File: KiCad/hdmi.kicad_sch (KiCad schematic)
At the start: 32 parts, among them J25 HDMI_A, Q1 2N7002, Q2 2N7002, Q3 2N7002, U20 H5VU25U, U21 H5VU25U, U22 H5VU25U

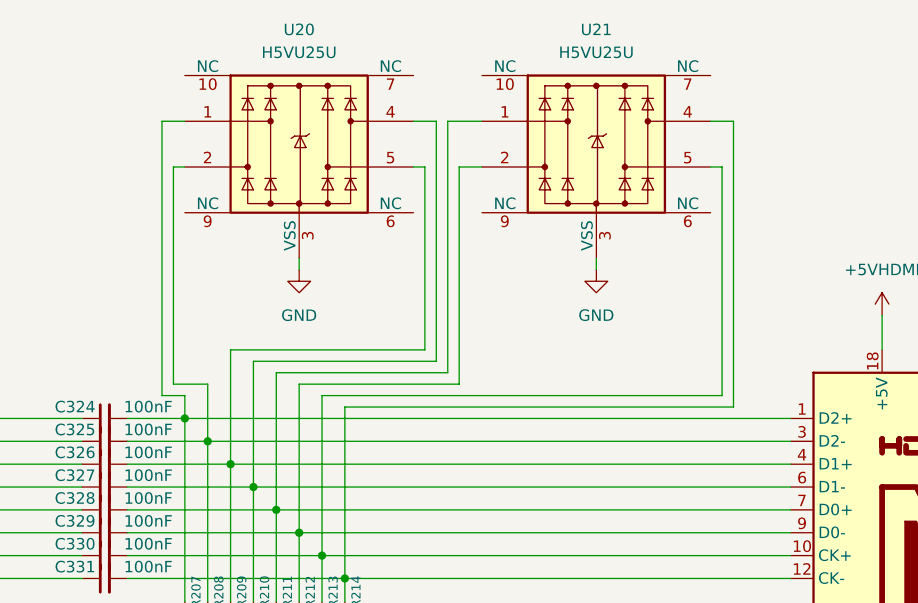
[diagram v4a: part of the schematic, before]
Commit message: Fix esd diodes, add some footprints.
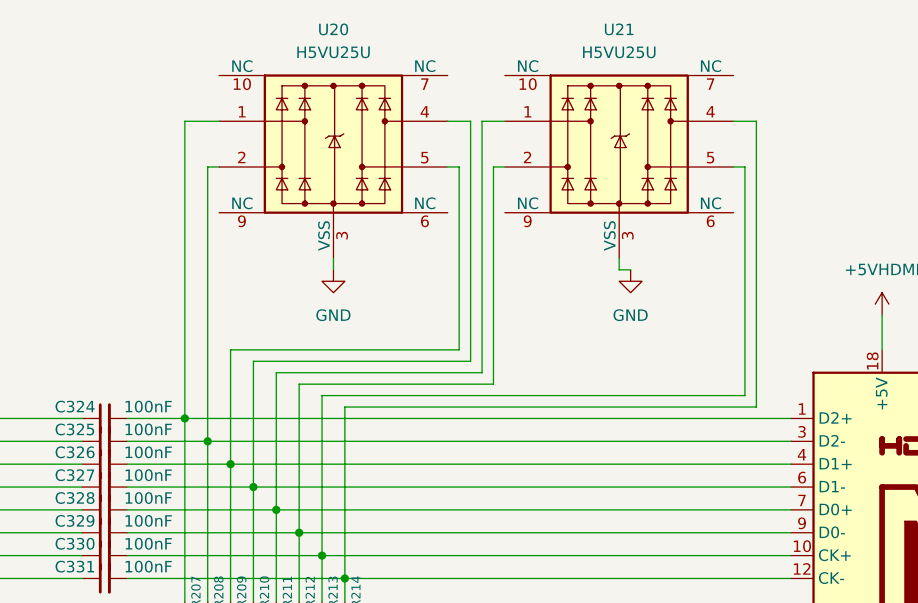
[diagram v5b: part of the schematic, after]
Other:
- moved on the sheet: U20, U21
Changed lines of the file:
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@@
 	(wire
 		(pts
-			(xy 198.12 62.23) (xy 198.12 63.5)
+			(xy 200.66 62.23) (xy 200.66 63.5)
 		)
 		(stroke
@@
 	(wire
 		(pts
-			(xy 181.61 74.93) (xy 162.56 74.93)
+			(xy 185.42 74.93) (xy 162.56 74.93)
 		)
 		(stroke
@@
 	(wire
 		(pts
-			(xy 212.09 77.47) (xy 167.64 77.47)
+			(xy 214.63 77.47) (xy 167.64 77.47)
+		)
+		(stroke
+			(width 0)
+			(type default)
+		)
+	)
+	(wire
+		(pts
+			(xy 200.66 63.5) (xy 201.93 63.5)
 		)
 		(stroke
@@
 	(wire
 		(pts
-			(xy 179.07 52.07) (xy 179.07 72.39)
+			(xy 182.88 52.07) (xy 182.88 72.39)
 		)
 		(stroke
@@
 	(wire
 		(pts
-			(xy 185.42 46.99) (xy 181.61 46.99)
+			(xy 187.96 46.99) (xy 185.42 46.99)
 		)
 		(stroke
@@
 	(wire
 		(pts
-			(xy 149.86 77.47) (xy 152.4 77.47)
-		)
-		(stroke
-			(width 0)
-			(type default)
-		)
-	)
-	(wire
-		(pts
 			(xy 146.05 97.79) (xy 170.18 97.79)
 		)
@@
 	(wire
 		(pts
-			(xy 177.8 52.07) (xy 179.07 52.07)
+			(xy 181.61 52.07) (xy 182.88 52.07)
 		)
 		(stroke
@@
 	(wire
 		(pts
-			(xy 179.07 72.39) (xy 157.48 72.39)
+			(xy 182.88 72.39) (xy 157.48 72.39)
 		)
 		(stroke
@@
 	(wire
 		(pts
-			(xy 210.82 46.99) (xy 213.36 46.99)
+			(xy 213.36 46.99) (xy 215.9 46.99)
 		)
 		(stroke
@@
 	(wire
 		(pts
-			(xy 152.4 77.47) (xy 152.4 80.01)
+			(xy 152.4 46.99) (xy 152.4 80.01)
 		)
 		(stroke
@@
 	(wire
 		(pts
-			(xy 213.36 46.99) (xy 213.36 78.74)
+			(xy 215.9 46.99) (xy 215.9 78.74)
 		)
 		(stroke
@@
 	(wire
 		(pts
-			(xy 149.86 46.99) (xy 149.86 77.47)
-		)
-		(stroke
-			(width 0)
-			(type default)
-		)
-	)
-	(wire
-		(pts
-			(xy 180.34 46.99) (xy 180.34 73.66)
+			(xy 184.15 46.99) (xy 184.15 73.66)
 		)
 		(stroke
@@
 	(wire
 		(pts
-			(xy 181.61 46.99) (xy 181.61 74.93)
+			(xy 185.42 46.99) (xy 185.42 74.93)
 		)
 		(stroke
@@
 	(wire
 		(pts
-			(xy 180.34 73.66) (xy 160.02 73.66)
+			(xy 184.15 73.66) (xy 160.02 73.66)
 		)
 		(stroke
@@
 	(wire
 		(pts
-			(xy 182.88 52.07) (xy 182.88 76.2)
+			(xy 186.69 52.07) (xy 186.69 76.2)
 		)
 		(stroke
@@
 	(wire
 		(pts
-			(xy 151.13 52.07) (xy 151.13 76.2)
-		)
-		(stroke
-			(width 0)
-			(type default)
-		)
-	)
-	(wire
-		(pts
-			(xy 185.42 52.07) (xy 182.88 52.07)
+			(xy 187.96 52.07) (xy 186.69 52.07)
 		)
 		(stroke
@@
 	(wire
 		(pts
-			(xy 165.1 62.23) (xy 165.1 63.5)
+			(xy 168.91 62.23) (xy 168.91 63.5)
 		)
 		(stroke
@@
 	(wire
 		(pts
-			(xy 151.13 76.2) (xy 154.94 76.2)
-		)
-		(stroke
-			(width 0)
-			(type default)
-		)
-	)
-	(wire
-		(pts
-			(xy 154.94 76.2) (xy 154.94 82.55)
+			(xy 154.94 52.07) (xy 154.94 82.55)
 		)
 		(stroke
@@
 	(wire
 		(pts
-			(xy 152.4 52.07) (xy 151.13 52.07)
+			(xy 156.21 52.07) (xy 154.94 52.07)
 		)
 		(stroke
@@
 	(wire
 		(pts
-			(xy 152.4 46.99) (xy 149.86 46.99)
+			(xy 156.21 46.99) (xy 152.4 46.99)
 		)
 		(stroke
@@
 	(wire
 		(pts
-			(xy 177.8 46.99) (xy 180.34 46.99)
+			(xy 181.61 46.99) (xy 184.15 46.99)
 		)
 		(stroke
@@
 	(wire
 		(pts
-			(xy 212.09 52.07) (xy 212.09 77.47)
+			(xy 214.63 52.07) (xy 214.63 77.47)
 		)
 		(stroke
@@
 	(wire
 		(pts
-			(xy 210.82 52.07) (xy 212.09 52.07)
+			(xy 213.36 52.07) (xy 214.63 52.07)
 		)
 		(stroke
@@
 	(wire
 		(pts
-			(xy 182.88 76.2) (xy 165.1 76.2)
+			(xy 186.69 76.2) (xy 165.1 76.2)
 		)
 		(stroke
@@
 	(wire
 		(pts
-			(xy 213.36 78.74) (xy 170.18 78.74)
+			(xy 215.9 78.74) (xy 170.18 78.74)
 		)
 		(stroke
@@
 	(symbol
 		(lib_id "power:GND")
-		(at 198.12 63.5 0)
+		(at 201.93 63.5 0)
 		(unit 1)
 		(exclude_from_sim no)
@@
 		(fields_autoplaced yes)
 		(property "Reference" "#PWR0317"
-			(at 198.12 69.85 0)
+			(at 201.93 69.85 0)
 			(effects
 				(font
@@
 		)
 		(property "Value" "GND"
-			(at 198.12 68.58 0)
+			(at 201.93 68.58 0)
 			(effects
 				(font
@@
 		)
 		(property "Footprint" ""
-			(at 198.12 63.5 0)
+			(at 201.93 63.5 0)
 			(effects
 				(font
@@
 		)
 		(property "Datasheet" ""
-			(at 198.12 63.5 0)
+			(at 201.93 63.5 0)
 			(effects
 				(font
@@
 		)
 		(property "Description" "Power symbol creates a global label with name \"GND\" , ground"
-			(at 198.12 63.5 0)
+			(at 201.93 63.5 0)
 			(effects
 				(font
@@
 	(symbol
 		(lib_id "Power_Protection:D3V3XA4B10LP")
-		(at 165.1 49.53 0)
+		(at 168.91 49.53 0)
 		(unit 1)
 		(exclude_from_sim no)
@@
 		(fields_autoplaced yes)
 		(property "Reference" "U20"
-			(at 165.1 36.83 0)
+			(at 168.91 36.83 0)
 			(effects
 				(font
@@
 		)
 		(property "Value" "H5VU25U"
-			(at 165.1 39.37 0)
+			(at 168.91 39.37 0)
 			(effects
 				(font
@@
 		)
 		(property "Footprint" "Package_DFN_QFN:Diodes_UDFN-10_1.0x2.5mm_P0.5mm"
-			(at 140.97 59.69 0)
+			(at 144.78 59.69 0)
 			(effects
 				(font
@@
 		)
 		(property "Datasheet" "https://www.diodes.com/assets/Datasheets/D3V3XA4B10LP.pdf"
-			(at 165.1 49.53 0)
+			(at 168.91 49.53 0)
 			(effects
 				(font
@@
 		)
 		(property "Description" "4-Channel Low Capacitance TVS Diode Array, DFN-10"
-			(at 165.1 49.53 0)
+			(at 168.91 49.53 0)
 			(effects
 				(font
@@
 	(symbol
 		(lib_id "Power_Protection:D3V3XA4B10LP")
-		(at 198.12 49.53 0)
+		(at 200.66 49.53 0)
 		(unit 1)
 		(exclude_from_sim no)
@@
 		(fields_autoplaced yes)
 		(property "Reference" "U21"
-			(at 198.12 36.83 0)
+			(at 200.66 36.83 0)
 			(effects
 				(font
@@
 		)
 		(property "Value" "H5VU25U"
-			(at 198.12 39.37 0)
+			(at 200.66 39.37 0)
 			(effects
 				(font
@@
 		)
 		(property "Footprint" "Package_DFN_QFN:Diodes_UDFN-10_1.0x2.5mm_P0.5mm"
-			(at 173.99 59.69 0)
+			(at 176.53 59.69 0)
 			(effects
 				(font
@@
 		)
 		(property "Datasheet" "https://www.diodes.com/assets/Datasheets/D3V3XA4B10LP.pdf"
-			(at 198.12 49.53 0)
+			(at 200.66 49.53 0)
 			(effects
 				(font
@@
 		)
 		(property "Description" "4-Channel Low Capacitance TVS Diode Array, DFN-10"
-			(at 198.12 49.53 0)
+			(at 200.66 49.53 0)
 			(effects
 				(font
@@
 	(symbol
 		(lib_id "power:GND")
-		(at 165.1 63.5 0)
+		(at 168.91 63.5 0)
 		(unit 1)
 		(exclude_from_sim no)
@@
 		(fields_autoplaced yes)
 		(property "Reference" "#PWR0316"
-			(at 165.1 69.85 0)
+			(at 168.91 69.85 0)
 			(effects
 				(font
@@
 		)
 		(property "Value" "GND"
-			(at 165.1 68.58 0)
+			(at 168.91 68.58 0)
 			(effects
 				(font
@@
 		)
 		(property "Footprint" ""
-			(at 165.1 63.5 0)
+			(at 168.91 63.5 0)
 			(effects
 				(font
@@
 		)
 		(property "Datasheet" ""
-			(at 165.1 63.5 0)
+			(at 168.91 63.5 0)
 			(effects
 				(font
@@
 		)
 		(property "Description" "Power symbol creates a global label with name \"GND\" , ground"
-			(at 165.1 63.5 0)
+			(at 168.91 63.5 0)
 			(effects
 				(font

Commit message: Lots of tiny capacitors
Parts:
- C323, C324, C325, C326, C327, C328, C329, C330, C331: footprint (none) -> Capacitor_SMD:C_0402_1005Metric
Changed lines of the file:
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@@
 			)
 		)
-		(property "Footprint" ""
+		(property "Footprint" "Capacitor_SMD:C_0402_1005Metric"
 			(at 143.51 85.09 0)
 			(effects
@@
 			)
 		)
-		(property "Footprint" ""
+		(property "Footprint" "Capacitor_SMD:C_0402_1005Metric"
 			(at 143.51 80.01 0)
 			(effects
@@
 			)
 		)
-		(property "Footprint" ""
+		(property "Footprint" "Capacitor_SMD:C_0402_1005Metric"
 			(at 143.51 90.17 0)
 			(effects
@@
 			)
 		)
-		(property "Footprint" ""
+		(property "Footprint" "Capacitor_SMD:C_0402_1005Metric"
 			(at 143.51 82.55 0)
 			(effects
@@
 			)
 		)
-		(property "Footprint" ""
+		(property "Footprint" "Capacitor_SMD:C_0402_1005Metric"
 			(at 143.51 87.63 0)
 			(effects
@@
 			)
 		)
-		(property "Footprint" ""
+		(property "Footprint" "Capacitor_SMD:C_0402_1005Metric"
 			(at 62.23 97.79 0)
 			(effects
@@
 			)
 		)
-		(property "Footprint" ""
+		(property "Footprint" "Capacitor_SMD:C_0402_1005Metric"
 			(at 143.51 92.71 0)
 			(effects
@@
 			)
 		)
-		(property "Footprint" ""
+		(property "Footprint" "Capacitor_SMD:C_0402_1005Metric"
 			(at 143.51 95.25 0)
 			(effects
@@
 			)
 		)
-		(property "Footprint" ""
+		(property "Footprint" "Capacitor_SMD:C_0402_1005Metric"
 			(at 143.51 97.79 0)
 			(effects

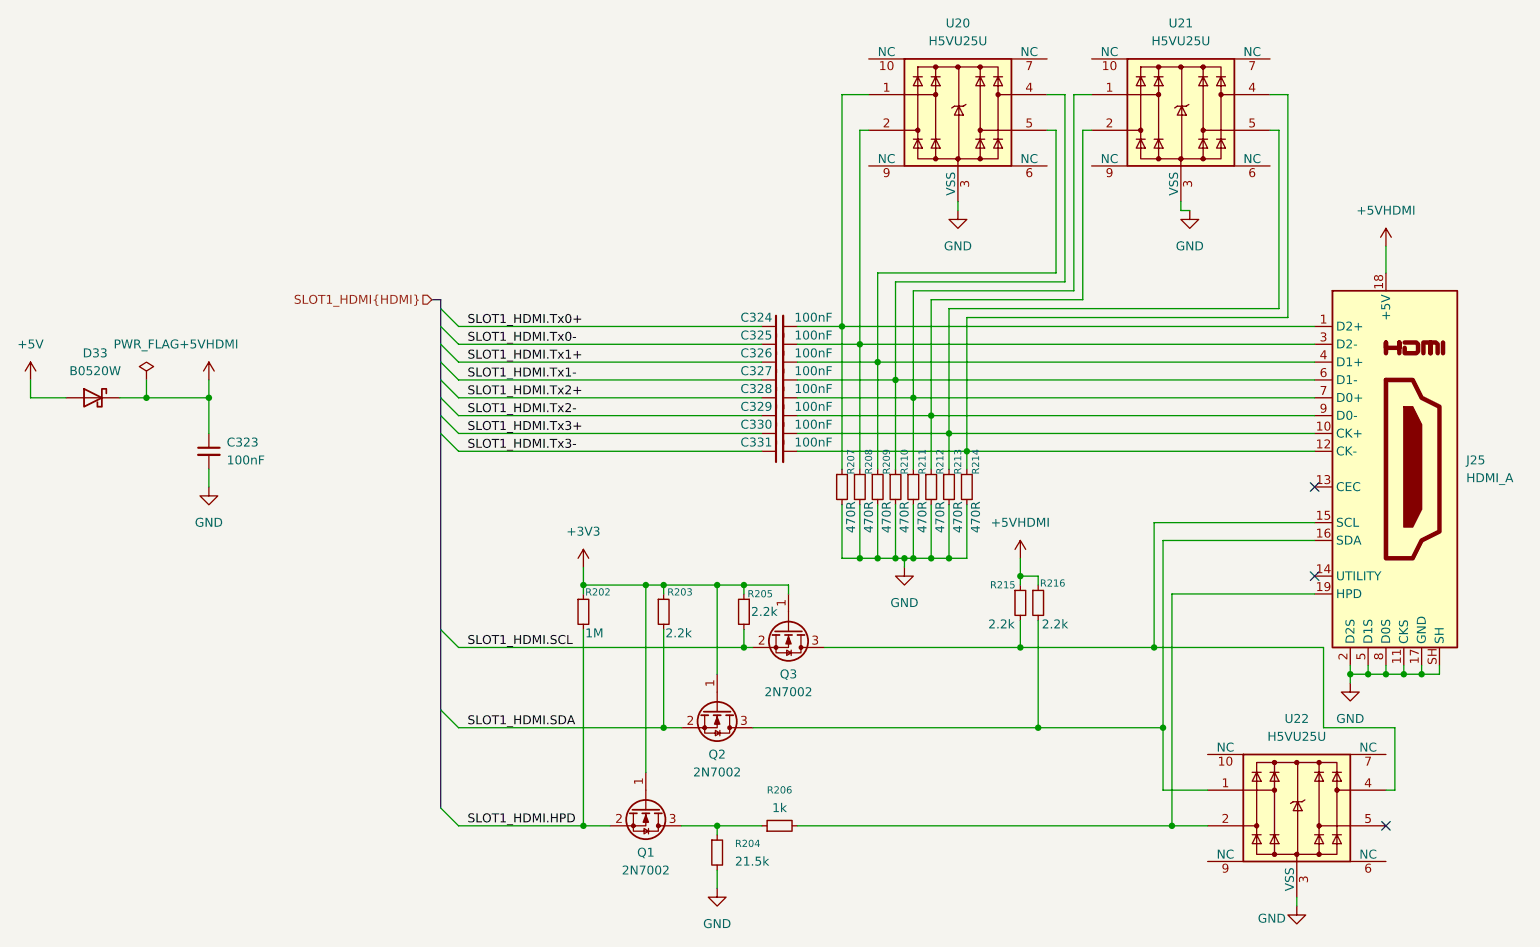
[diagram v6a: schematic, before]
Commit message: Add most passive component footprints
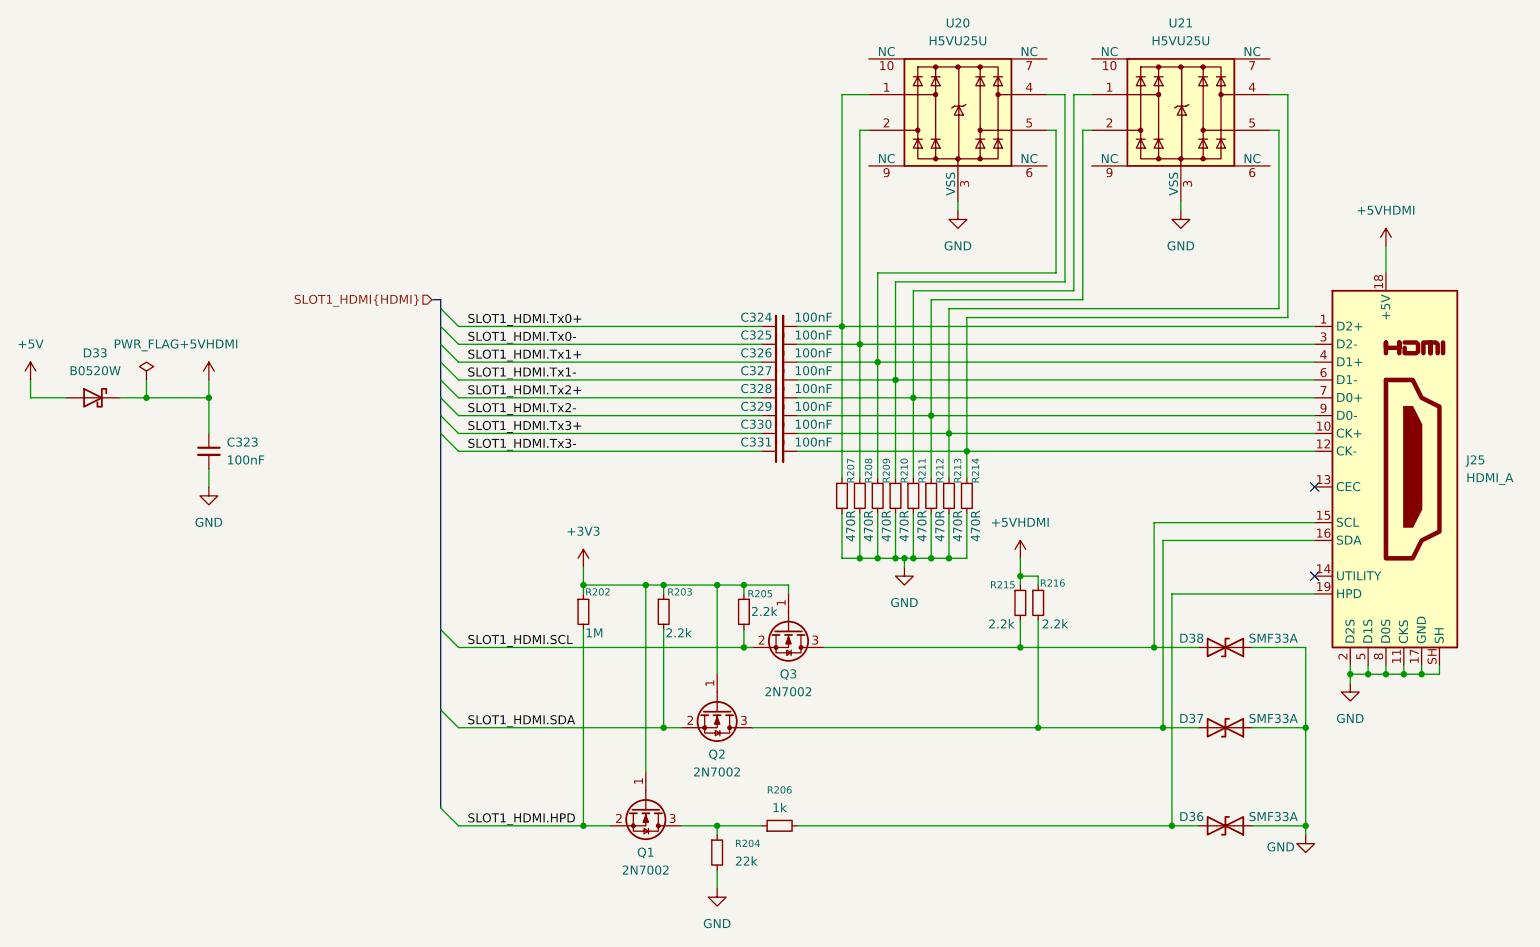
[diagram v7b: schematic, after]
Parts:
- removed U22: H5VU25U, Package_DFN_QFN:Diodes_UDFN-10_1.0x2.5mm_P0.5mm, symbol Power_Protection:D3V3XA4B10LP
- added D36, D37, D38: SMF33A, Diode_SMD:D_SOD-123F, symbol Device:D_TVS
- D33: footprint (none) -> Diode_SMD:D_SOD-123
- Q1, Q2, Q3: footprint (none) -> Package_TO_SOT_SMD:SOT-23
- R202, R203, R205, R207, R208, R209, R210, R211, R212, R213, R214, R215, R216: footprint (none) -> Resistor_SMD:R_0402_1005Metric
- R204: value 21.5k -> 22k; footprint (none) -> Resistor_SMD:R_0402_1005Metric
- R206: footprint (none) -> Resistor_SMD:R_0805_2012Metric
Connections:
- net GND: now also D36.1 (A1), D37.1 (A1), D38.1 (A1)
- net at J25.16 (SDA), Q2.3 (D), R216.2: now also D37.2 (A2)
- net at J25.19 (HPD), R206.2: now also D36.2 (A2)
- net at J25.15 (SCL), Q3.3 (D), R215.2: now also D38.2 (A2)
- no-connect marks 3 -> 2
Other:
- moved on the sheet: R207, R208, R209, R210, R211, R212, R213, R214

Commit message: Add m.2 slot footprints
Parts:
- J25: footprint (none) -> Connector_Video:HDMI_A_Molex_208658-1001_Horizontal
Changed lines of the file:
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@@
 			)
 		)
-		(property "Footprint" ""
+		(property "Footprint" "Connector_Video:HDMI_A_Molex_208658-1001_Horizontal"
 			(at 230.505 100.33 0)
 			(effects
